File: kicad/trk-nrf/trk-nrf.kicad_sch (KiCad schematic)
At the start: 46 parts, among them J1 Conn_02x05_Odd_Even, J2 Conn_01x20_Pin, U1 nRF9151-LAXX, U2 CDCE6214RGER, U3 TPS631010YBGR, U4 TPS631010YBGR, X1 TG2520SMN-xx.xxxxxxMhz-xxxxNM

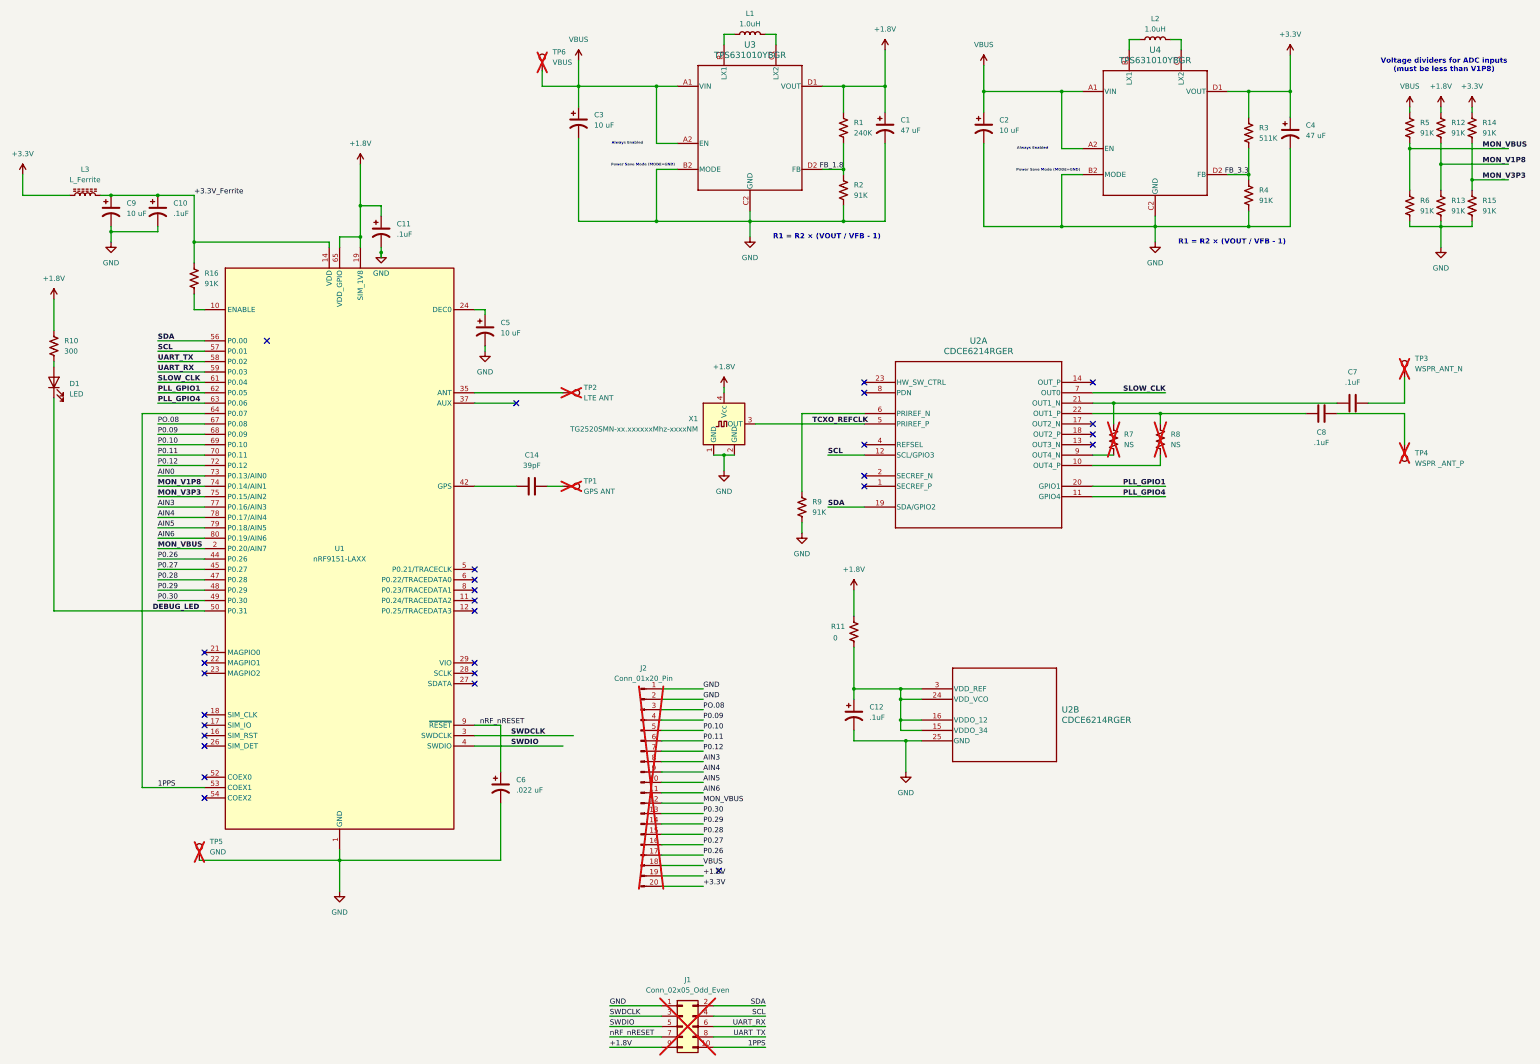
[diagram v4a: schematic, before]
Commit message: Board detailed routing by Estifanos Nega
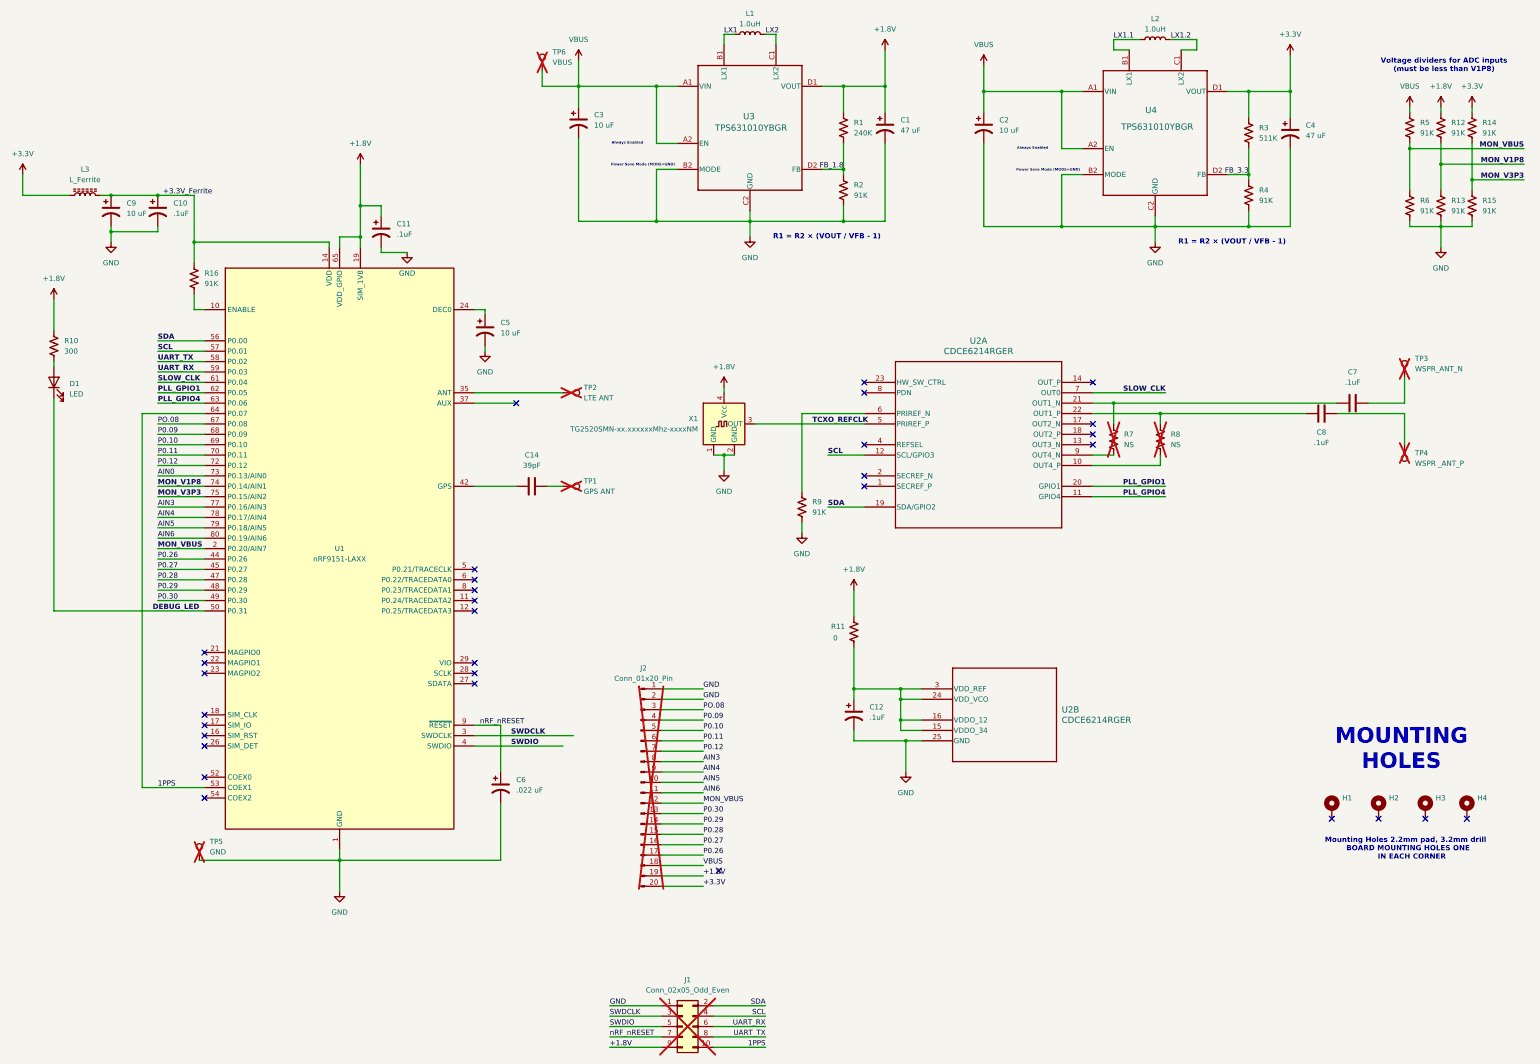
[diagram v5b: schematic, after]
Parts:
- added H1, H2, H3, H4: MountingHole_Pad_MP, MountingHole:MountingHole_2.2mm_M2_ISO7380_Pad, symbol Mechanical:MountingHole_Pad_MP
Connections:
- net LX1.1: now reaches L2.1, U4.B1 (LX1)
- net LX1.2: now reaches L2.2, U4.C1 (LX2)
- net LX1: now reaches L1.1, U3.B1 (LX1)
- net LX2: now reaches L1.2, U3.C1 (LX2)
- no-connect marks 29 -> 32
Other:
- note added: "MOUNTING HOLES"
- note added: "Mounting Holes 2.2mm pad, 3.2mm drill BOARD MOUNTING HOLES ONE IN EACH CORNER"
